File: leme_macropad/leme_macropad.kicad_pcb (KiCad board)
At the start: 4 copper layers, 99.9 x 63.9 mm, 93 parts, among them J1 USB_C_Receptacle_USB2.0_16P, J2 OLED display, SW1 SW_Push, SW10 SW_Push, SW2 SW_Push, SW3 SW_Push, SW4 SW_Push, SW5 SW_Push, SW6 SW_Push, SW7 RotaryEncoder_Switch, SW9 SW_Push, U2 NCP1117-3.3_SOT223, U3 W25Q128JVS, U4 RP2040, U5 USBLC6-2SC6, Y1 ABM8-272-T3

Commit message: Removes unused tespoints
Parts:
- removed TP20, TP4, TP5: TestPoint, TestPoint:TestPoint_Pad_D1.0mm

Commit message: Reassigns designators based on component location on the PCB
Kicad 6 has a tool for that: geographical reannotate.
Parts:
- renumbered C4 to C0, C12 to C1, C11 to C10, C10 to C11, C13 to C12, C15 to C13, C6 to C15, C7 to C16, C5 to C2, C16 to C3, C17 to C4, C3 to C5, C1 to C6, C8 to C7, C2 to C8, D11 to D1, D3 to D10, D1 to D11, D7 to D12, D6 to D13, D4 to D14, D2 to D15, D10 to D2, D9 to D3, D15 to D4, D16 to D5, D12 to D6, D13 to D7, D14 to D8, D5 to D9, J2 to J1, J1 to J2, R5 to R0, R11 to R1, R9 to R10, R4 to R3, R1 to R4, R6 to R5, R7 to R6, R3 to R7, R10 to R9, SW3 to SW2, SW5 to SW3, SW7 to SW4, SW2 to SW5, SW4 to SW6, SW6 to SW7, SW10 to SW8, TP8 to TP0, TP6 to TP1, TP23 to TP10, TP3 to TP11, TP2 to TP12, TP1 to TP13, TP19 to TP14, TP12 to TP15, TP11 to TP16, TP25 to TP17, TP9 to TP18, TP13 to TP19, TP7 to TP2, TP16 to TP20, TP15 to TP21, TP14 to TP22, TP18 to TP23, TP17 to TP24, TP10 to TP25, TP27 to TP3, TP26 to TP4, TP29 to TP5, TP28 to TP6, TP22 to TP7, TP21 to TP8, TP24 to TP9, U3 to U0, U5 to U1, U4 to U3, Y1 to Y0

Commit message: Small adjustments
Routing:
- net GND: track 58.4 -> 72.2 mm, vias 36 -> 40
- net Net-(D15-DOUT): track 37.9 -> 30.2 mm
- net ROW 2: track 125.2 -> 122.8 mm
- net Encoder DT: track 39.3 -> 38.1 mm
- net SWDIO: track 19.6 -> 18.8 mm

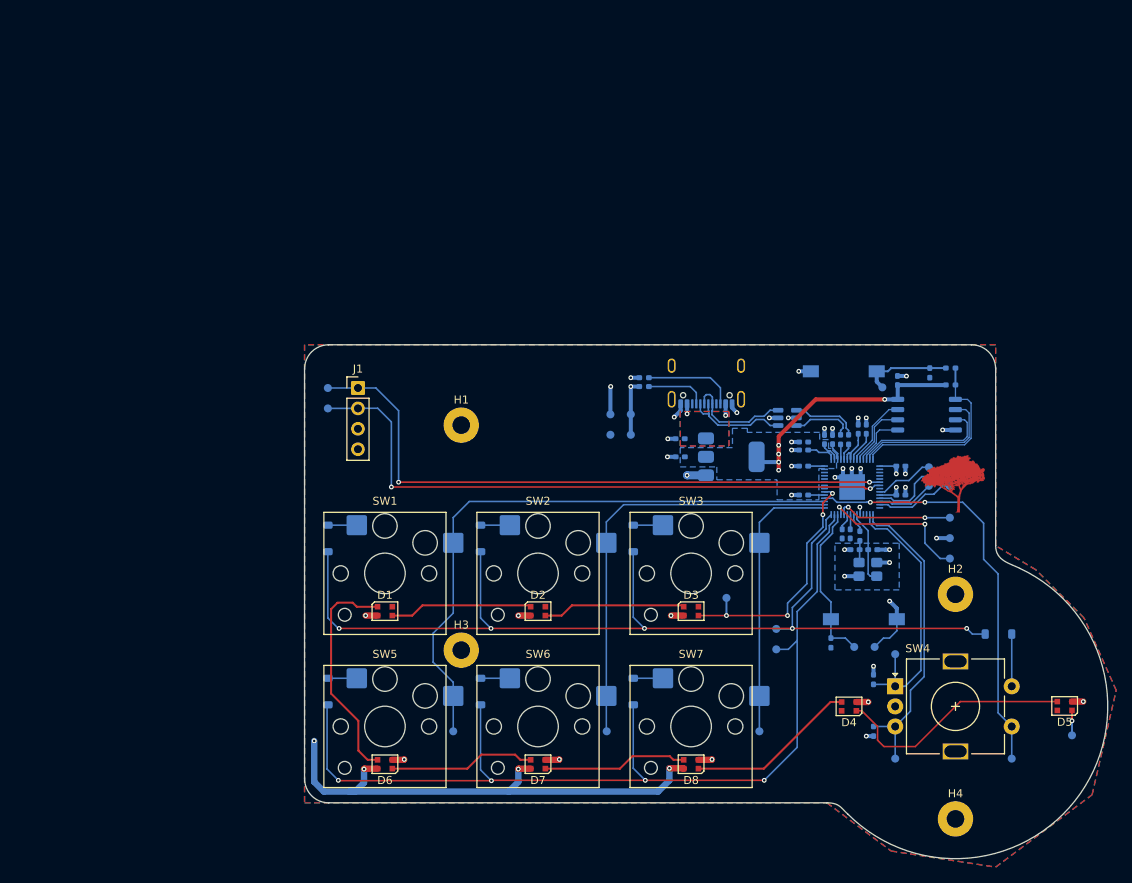
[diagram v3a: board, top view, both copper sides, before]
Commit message: Deletes all tracks and vias to start from scratch
This also removes the 3v3 and 5V planes.
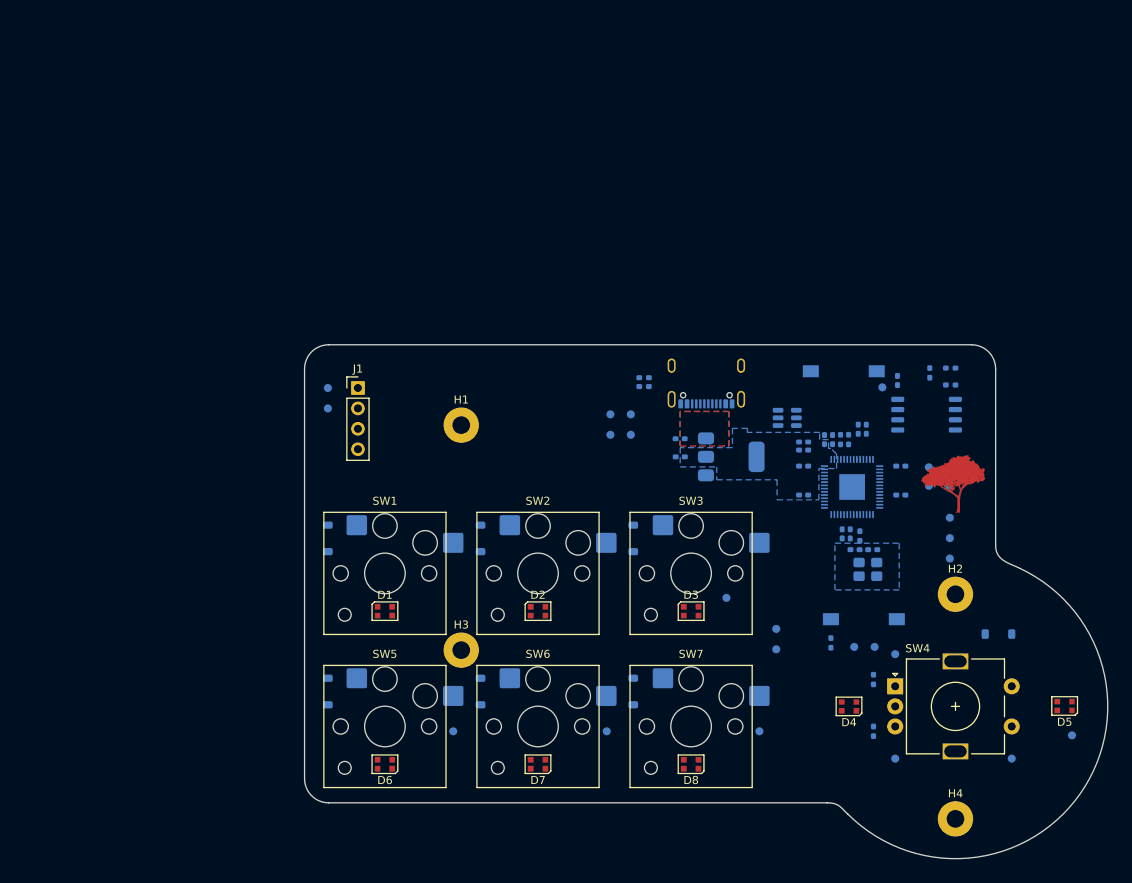
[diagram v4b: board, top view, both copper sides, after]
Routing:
- net ROW 1: track 129.3 -> 0.00 mm, vias 5 -> 0
- net ROW 2: track 122.8 -> 0.00 mm, vias 4 -> 0
- net I2C0_SDA: track 78.7 -> 0.00 mm, vias 2 -> 0
- net I2C0_SCL: track 77.7 -> 0.00 mm, vias 2 -> 0
- net COL 1: track 75.7 -> 0.00 mm
- net GND: track 72.2 -> 0.00 mm, vias 40 -> 0
- net +5V: track 71.4 -> 0.00 mm, vias 8 -> 0
- net +3.3V: track 57.4 -> 0.00 mm, vias 9 -> 0
- net COL 2: track 54.1 -> 0.00 mm
- net COL 4: track 51.8 -> 0.00 mm, vias 2 -> 0
- net Encoder DT: track 38.1 -> 0.00 mm
- net COL 3: track 34.8 -> 0.00 mm
- net Encoder CLK: track 33.7 -> 0.00 mm
- net LED_DATA_IN: track 31.9 -> 0.00 mm, vias 4 -> 0
- net Net-(D15-DOUT): track 30.2 -> 0.00 mm
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
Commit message: Separates out logical groups of components so we can reorganize them
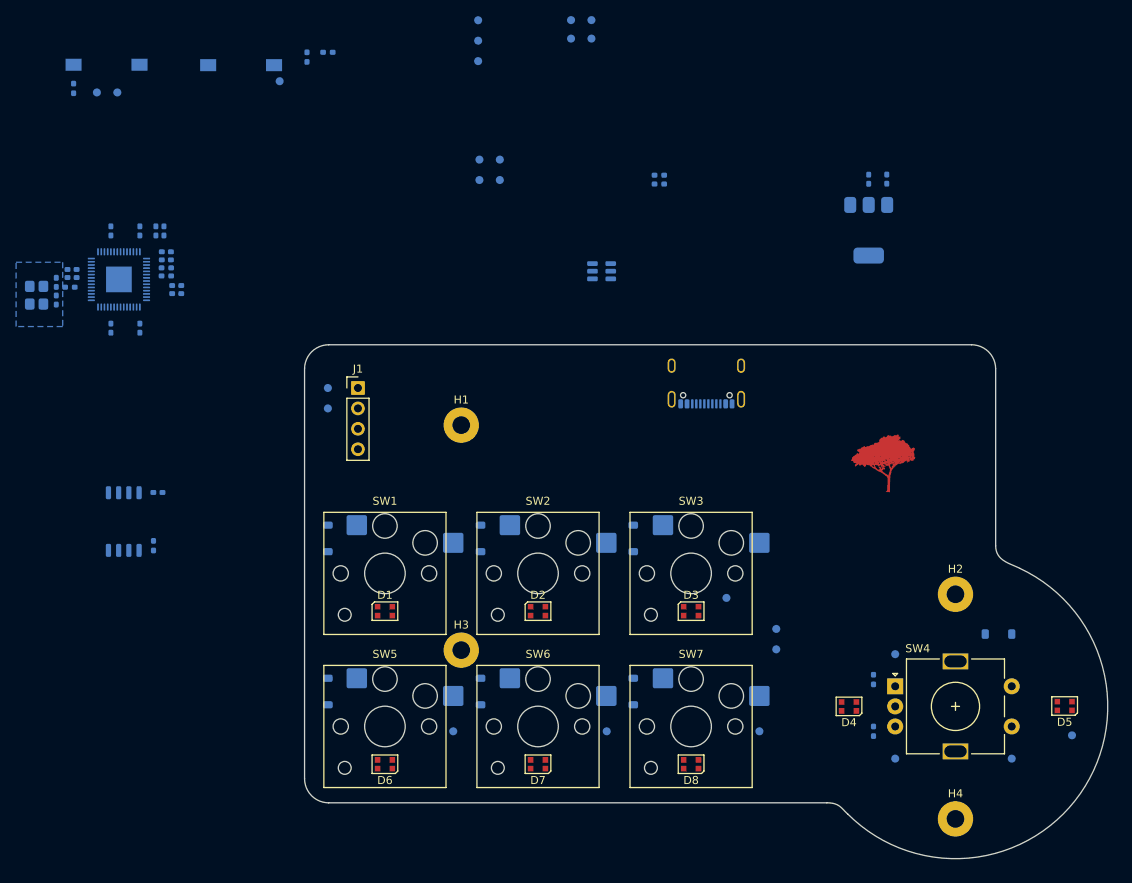
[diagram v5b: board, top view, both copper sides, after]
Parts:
- moved R8 116.8 mm to (80.3, 33.1)
- moved SW9 116.8 mm to (84.4, 30.1)
- moved TP17 116.8 mm to (85.7, 33.6)
- moved TP18 116.8 mm to (83.2, 33.6)
- moved Y0 108.9 mm to (75.7, 58.8), turned to 90 degrees
- moved C15 106.2 mm to (78.1, 59.4), turned to 90 degrees
- moved C16 104.8 mm to (78.1, 57.2), turned to -90 degrees
- moved R7 103.1 mm to (79.8, 57.8), turned to 0 degrees
- moved C13 102.0 mm to (80.1, 56.6), turned to 180 degrees
- moved C14 101.3 mm to (80.1, 55.6), turned to 180 degrees
- moved R3 101.2 mm to (90.2, 90.0), turned to 90 degrees
- moved U0 100.8 mm to (86.5, 87.0), turned to 90 degrees
- moved C11 100.5 mm to (84.9, 62.9), turned to -90 degrees
- moved C9 96.2 mm to (88.5, 62.9), turned to -90 degrees
- moved U3 94.8 mm to (85.9, 56.9), turned to 90 degrees
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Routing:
- removed copper zone on B.Cu, net +3.3V
- removed copper zone on B.Cu, net +5V
- removed copper zone on F.Cu, net +5V

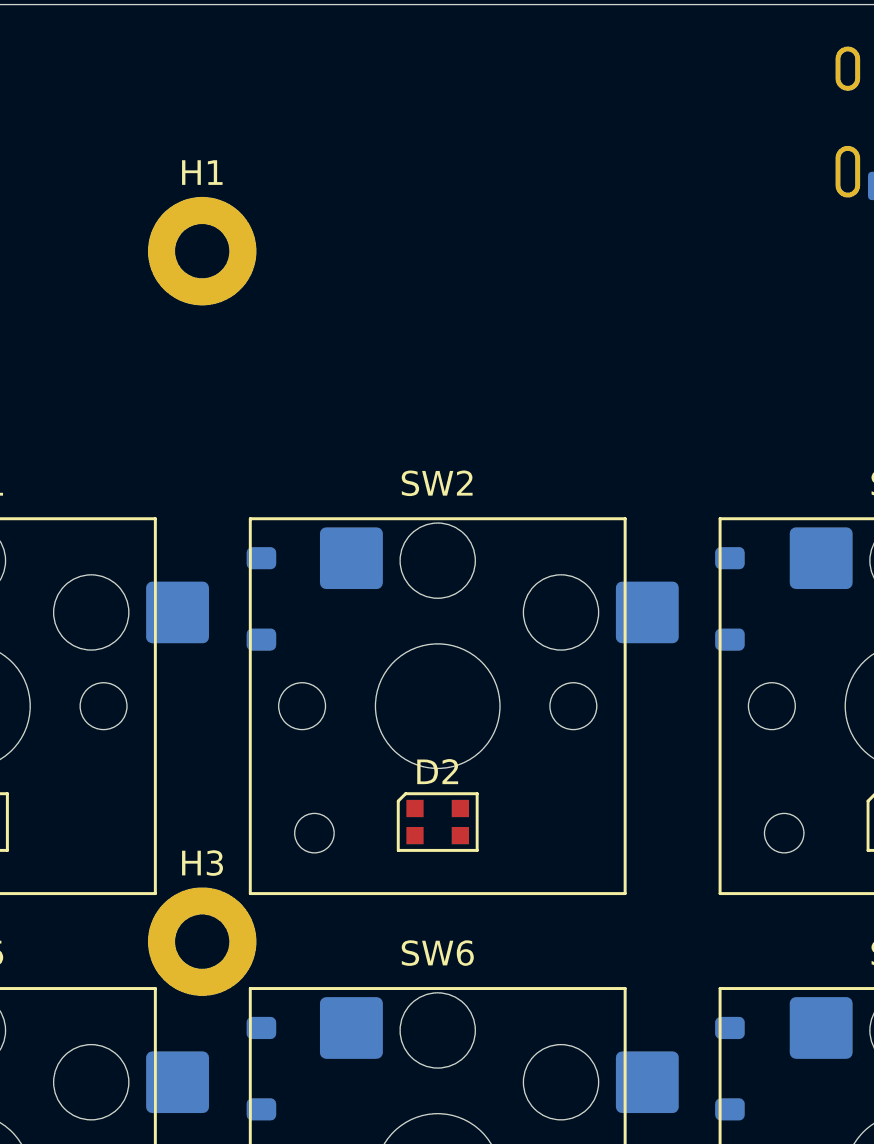
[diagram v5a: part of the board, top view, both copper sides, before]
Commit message: Moves screw hole to open more space for routing
This will also add more support to the buttons, albeit at the expense of
losing some under de display connect. Because the display will likely
not be connected and disconnected often, this should be ok.
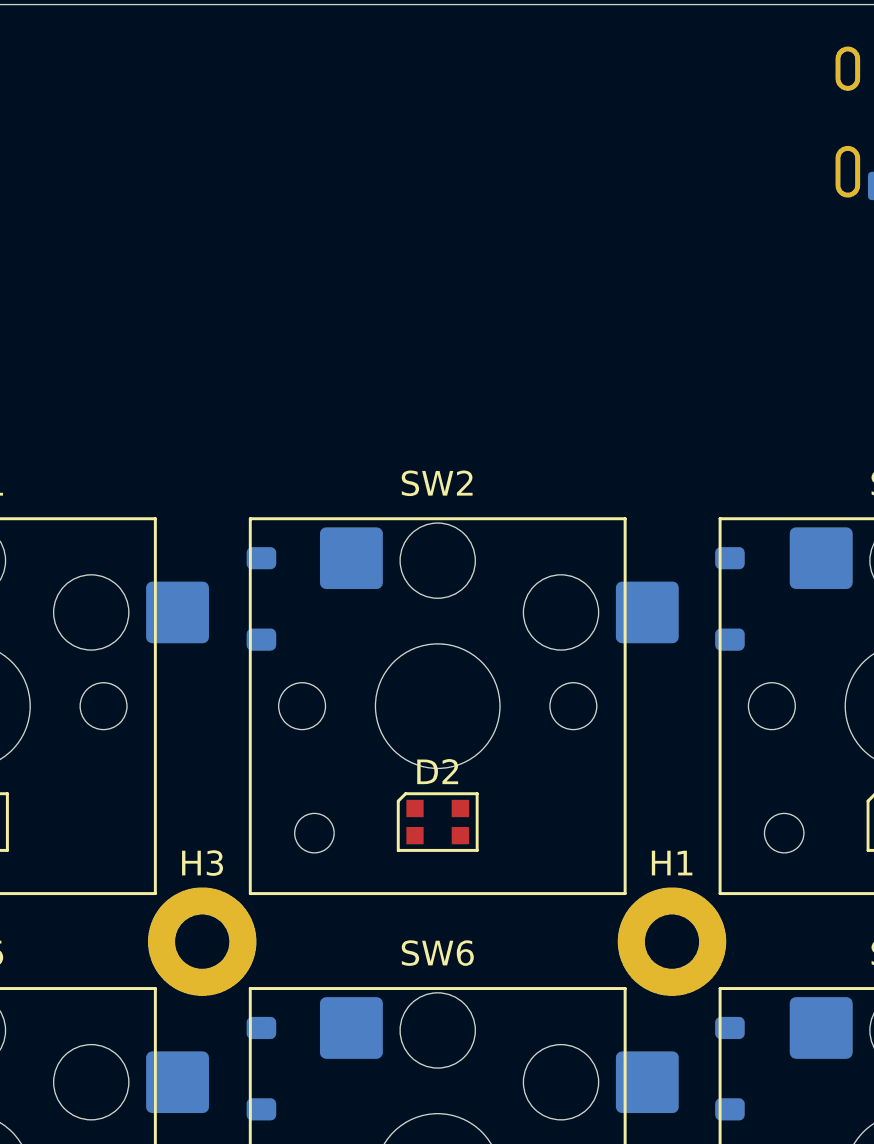
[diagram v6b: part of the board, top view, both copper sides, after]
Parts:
- moved H1 33.9 mm to (147.6, 103.0)
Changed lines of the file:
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@@
 		(locked yes)
 		(layer "F.Cu")
-		(at 128.5 75)
+		(at 147.55 103)
 		(descr "Mounting Hole 2.2mm, M2, generated by kicad-footprint-generator mountinghole.py")
 		(tags "mountinghole M2")

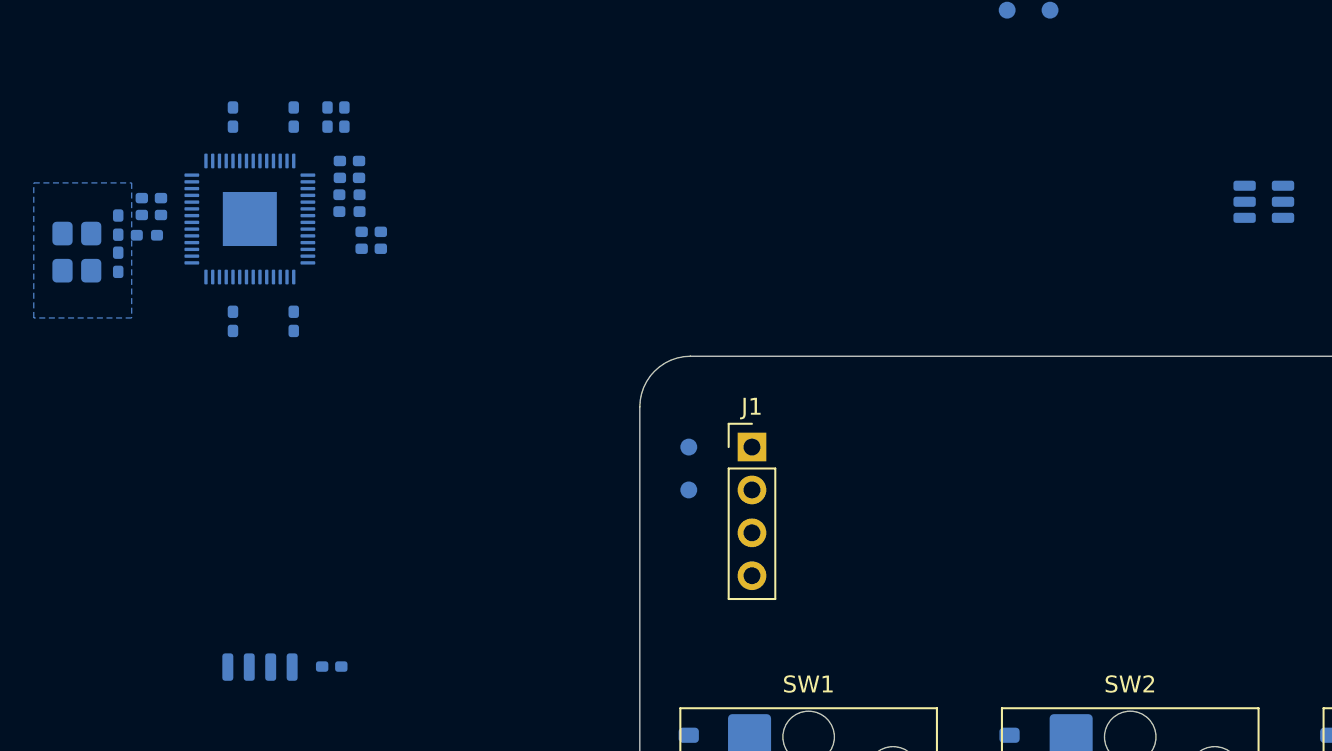
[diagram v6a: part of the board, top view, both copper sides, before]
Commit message: Routes RP2040 power
This is basically a copy of the reference RP2040 design. Ground
connections are still missing, even in the center pad, mainly because
this footprint doesn't include vias.
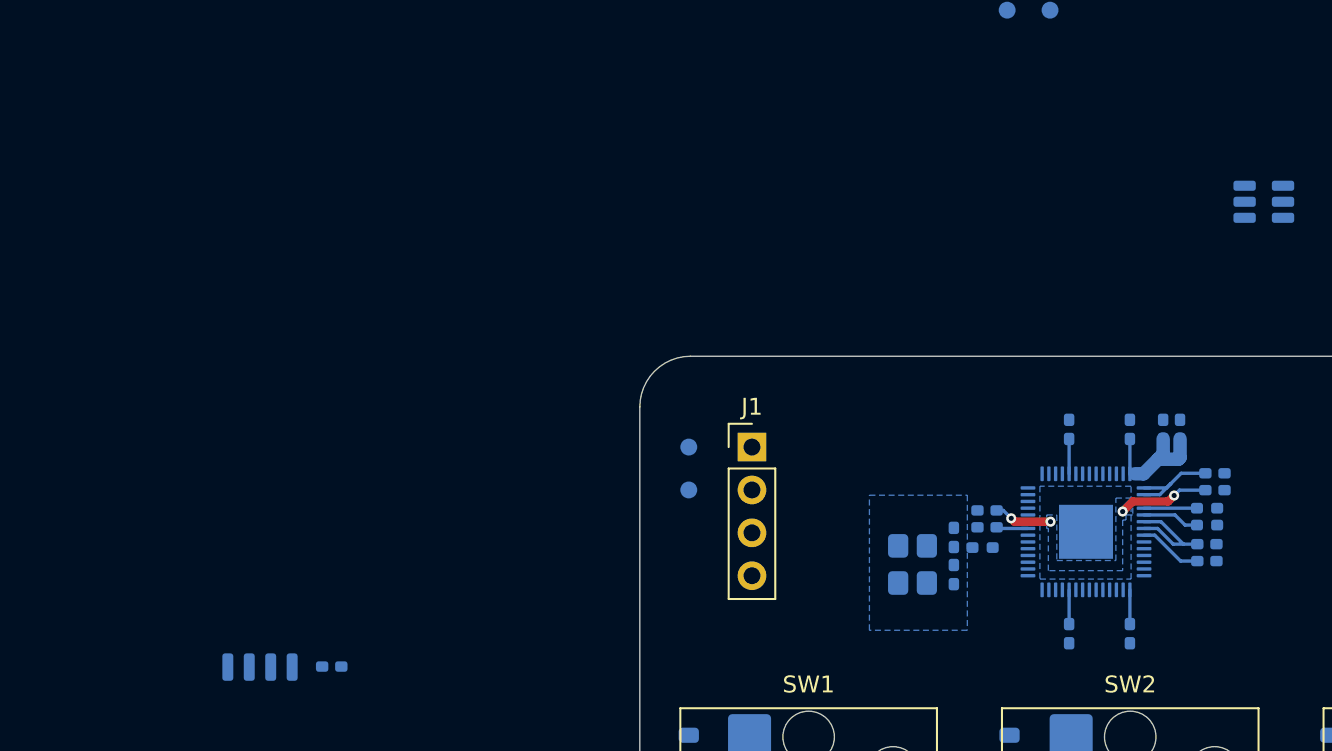
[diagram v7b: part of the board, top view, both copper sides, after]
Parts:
- moved C3 54.5 mm to (143.1, 72.9)
- moved C4 54.5 mm to (143.1, 71.9)
- moved R5 54.1 mm to (142.6, 75.0)
- moved R6 54.1 mm to (142.6, 74.0)
- moved U3 52.9 mm to (135.4, 75.4)
- moved C11 52.9 mm to (134.4, 81.4)
- moved C9 52.9 mm to (138.0, 81.4)
- moved C10 52.9 mm to (138.0, 69.3)
- moved C12 52.9 mm to (134.4, 69.3)
- moved C13 52.8 mm to (129.6, 75.1)
- moved C14 52.8 mm to (129.6, 74.1)
- moved C15 52.8 mm to (127.6, 77.9)
- moved C16 52.8 mm to (127.6, 75.7)
- moved C5 52.8 mm to (141.0, 69.3)
- moved C7 52.8 mm to (140.0, 69.3)
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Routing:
- net +3.3V: track 0.00 -> 27.8 mm
- net +1V1: track 0.00 -> 17.3 mm, vias 0 -> 4
- net /microcontroller/uC_D+: track 0.00 -> 3.38 mm
- net /microcontroller/uC_D-: track 0.00 -> 3.13 mm
- added copper zone on B.Cu, net +1V1
- added copper zone on B.Cu, net +3.3V
- removed copper zone on In1.Cu, net GND
- removed copper zone on In2.Cu, net GND
